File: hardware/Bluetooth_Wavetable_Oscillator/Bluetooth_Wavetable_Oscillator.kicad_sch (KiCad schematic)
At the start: 6 parts, among them U2 ESP32-C6-DevKitC-1, U3 MCP4821

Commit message: add audio test files
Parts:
- C15, C7, C8: footprint (none) -> Capacitor_THT:C_Disc_D5.0mm_W2.5mm_P5.00mm
- U3: footprint (none) -> Package_DIP:DIP-8_W7.62mm
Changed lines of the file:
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@@
 			)
 		)
-		(property "Footprint" ""
+		(property "Footprint" "Capacitor_THT:C_Disc_D5.0mm_W2.5mm_P5.00mm"
 			(at 56.8452 50.8 0)
 			(effects
@@
 			)
 		)
-		(property "Footprint" ""
+		(property "Footprint" "Package_DIP:DIP-8_W7.62mm"
 			(at 102.87 156.21 0)
 			(effects
@@
 			)
 		)
-		(property "Footprint" ""
+		(property "Footprint" "Capacitor_THT:C_Disc_D5.0mm_W2.5mm_P5.00mm"
 			(at 90.17 138.7348 0)
 			(effects
@@
 			)
 		)
-		(property "Footprint" ""
+		(property "Footprint" "Capacitor_THT:C_Disc_D5.0mm_W2.5mm_P5.00mm"
 			(at 211.7852 67.31 0)
 			(effects

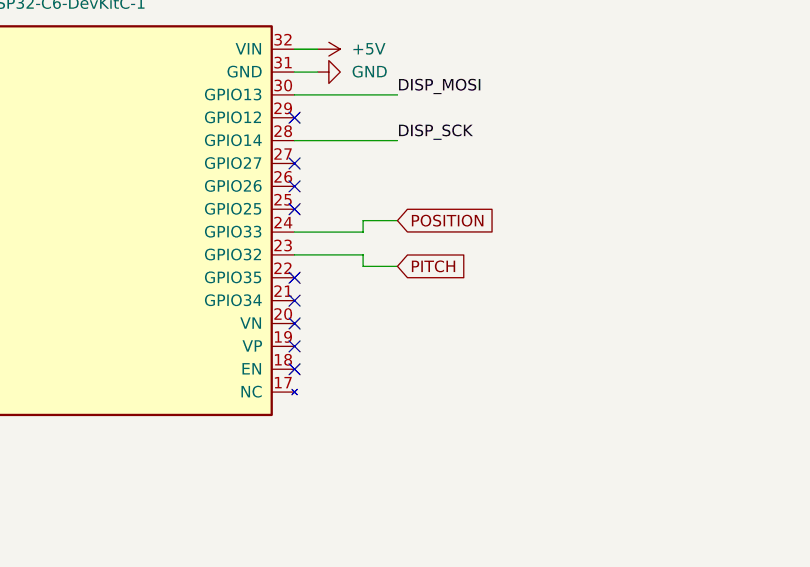
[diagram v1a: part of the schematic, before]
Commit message: change ADC input pins in schematic
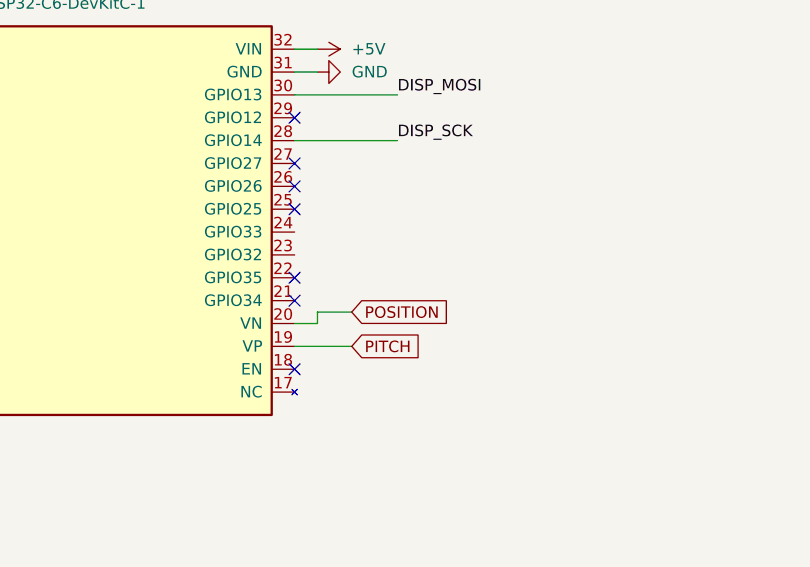
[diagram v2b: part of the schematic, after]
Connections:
- net PITCH: now also U2.19 (VP); no longer U2.23 (GPIO32)
- net POSITION: now also U2.20 (VN); no longer U2.24 (GPIO33)
- no-connect marks 16 -> 14
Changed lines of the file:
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@@
-	)
-	(no_connect
-		(at 109.22 83.82)
 	)
 	(no_connect
@@
 	)
 	(no_connect
-		(at 109.22 86.36)
-	)
-	(no_connect
 		(at 109.22 68.58)
 	)
 	(wire
 		(pts
+			(xy 109.22 86.36) (xy 115.57 86.36)
+		)
+		(stroke
+			(width 0)
+			(type default)
+		)
+	)
+	(wire
+		(pts
 			(xy 45.72 158.75) (xy 67.31 158.75)
 		)
@@
 	(wire
 		(pts
-			(xy 109.22 76.2) (xy 116.84 76.2)
-		)
-		(stroke
-			(width 0)
-			(type default)
-		)
-	)
-	(wire
-		(pts
 			(xy 109.22 58.42) (xy 120.65 58.42)
 		)
@@
 	(wire
 		(pts
+			(xy 111.76 82.55) (xy 111.76 83.82)
+		)
+		(stroke
+			(width 0)
+			(type default)
+		)
+	)
+	(wire
+		(pts
 			(xy 55.88 40.64) (xy 55.88 43.18)
 		)
@@
 	(wire
 		(pts
-			(xy 116.84 73.66) (xy 109.22 73.66)
-		)
-		(stroke
-			(width 0)
-			(type default)
-		)
-	)
-	(wire
-		(pts
 			(xy 95.25 153.67) (xy 104.14 153.67)
 		)
@@
 	(wire
 		(pts
-			(xy 116.84 76.2) (xy 116.84 77.47)
+			(xy 111.76 83.82) (xy 109.22 83.82)
 		)
 		(stroke
@@
 	(wire
 		(pts
-			(xy 116.84 72.39) (xy 120.65 72.39)
-		)
-		(stroke
-			(width 0)
-			(type default)
-		)
-	)
-	(wire
-		(pts
 			(xy 53.34 53.34) (xy 55.88 53.34)
 		)
@@
 	(wire
 		(pts
-			(xy 116.84 77.47) (xy 120.65 77.47)
-		)
-		(stroke
-			(width 0)
-			(type default)
-		)
-	)
-	(wire
-		(pts
 			(xy 213.36 83.82) (xy 226.06 83.82)
 		)
@@
 	(wire
 		(pts
+			(xy 115.57 82.55) (xy 111.76 82.55)
+		)
+		(stroke
+			(width 0)
+			(type default)
+		)
+	)
+	(wire
+		(pts
 			(xy 55.88 53.34) (xy 58.42 53.34)
 		)
@@
 		(pts
 			(xy 80.01 139.7) (xy 82.55 139.7)
-		)
-		(stroke
-			(width 0)
-			(type default)
-		)
-	)
-	(wire
-		(pts
-			(xy 116.84 72.39) (xy 116.84 73.66)
 		)
 		(stroke
@@
 	(global_label "POSITION"
 		(shape input)
-		(at 120.65 72.39 0)
+		(at 115.57 82.55 0)
 		(fields_autoplaced yes)
 		(effects
@@
 		)
 		(property "Intersheetrefs" "${INTERSHEET_REFS}"
-			(at 132.2834 72.39 0)
+			(at 127.2034 82.55 0)
 			(effects
 				(font
@@
 	(global_label "PITCH"
 		(shape input)
-		(at 120.65 77.47 0)
+		(at 115.57 86.36 0)
 		(fields_autoplaced yes)
 		(effects
@@
 		)
 		(property "Intersheetrefs" "${INTERSHEET_REFS}"
-			(at 129.0781 77.47 0)
+			(at 123.9981 86.36 0)
 			(effects
 				(font

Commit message: add bth components, add component values, update SPI pins, change disp power supply to 5V
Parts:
- added D7: LED, symbol Device:LED
- added R23: R, symbol Device:R
- added SW1: SW_Push, symbol Switch:SW_Push
- C15: value C -> 0.1u
- U2: value ESP32-C6-DevKitC-1 -> ESP32-WROOM-32D
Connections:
- net +3.3V: no longer C15.2, DISP1.2 (VDD)
- net +5V: now also C15.2, DISP1.2 (VDD)
- net DAC_CS: now also U2.3 (GPIO15); no longer U2.8 (GPIO5)
- net DAC_MOSI: now also U2.30 (GPIO13); no longer U2.15 (GPIO23)
- net DAC_SCK: now also U2.28 (GPIO14); no longer U2.9 (GPIO18)
- net DISP_CS: now also U2.8 (GPIO5); no longer U2.3 (GPIO15)
- net DISP_MOSI: now also U2.15 (GPIO23); no longer U2.30 (GPIO13)
- net DISP_SCK: now also U2.9 (GPIO18); no longer U2.28 (GPIO14)
- net GND: now also R23.2, SW1.1
- net BTH_LED: now reaches U2.14 (GPIO22)
- net BTH_LED: now also D7.2 (A)
- net BTH_SWITCH: now reaches U2.5 (GPIO4)
- net BTH_SWITCH: now also SW1.2
- new net: D7.1 (K), R23.1
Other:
- moved on the sheet: C15

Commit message: start PCB layout
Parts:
- D7: footprint (none) -> Diode_THT:D_A-405_P2.54mm_Vertical_AnodeUp
- DISP1: footprint (none) -> 1.5inch_RGB_OLED_Module:1.5inch_RGB_OLED_Module
- R23: value R -> 220R; footprint (none) -> Resistor_THT:R_Axial_DIN0204_L3.6mm_D1.6mm_P2.54mm_Vertical
- SW1: footprint (none) -> 6Pin-Switch-Button:6Pin-Switch-Button
- U2: footprint (none) -> ESP32:ESP32
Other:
- title: Microcontroller, DAC, Display -> Microcontroller, DAC, Display, BTH Switch/LED
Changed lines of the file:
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@@
 	(paper "A4")
 	(title_block
-		(title "Microcontroller, DAC, Display")
+		(title "Microcontroller, DAC, Display, BTH Switch/LED")
 		(date "2024-11-18")
 		(rev "1")
@@
 			)
 		)
-		(property "Footprint" ""
+		(property "Footprint" "1.5inch_RGB_OLED_Module:1.5inch_RGB_OLED_Module"
 			(at 232.41 72.39 0)
 			(effects
@@
 			)
 		)
-		(property "Footprint" ""
+		(property "Footprint" "ESP32:ESP32"
 			(at 83.82 96.52 0)
 			(effects
@@
 			)
 		)
-		(property "Value" "R"
+		(property "Value" "220R"
 			(at 234.95 135.89 90)
 			(effects
@@
 			)
 		)
-		(property "Footprint" ""
+		(property "Footprint" "Resistor_THT:R_Axial_DIN0204_L3.6mm_D1.6mm_P2.54mm_Vertical"
 			(at 234.95 141.478 90)
 			(effects
@@
 			)
 		)
-		(property "Footprint" ""
+		(property "Footprint" "Diode_THT:D_A-405_P2.54mm_Vertical_AnodeUp"
 			(at 222.25 139.7 0)
 			(effects
@@
 			)
 		)
-		(property "Footprint" ""
+		(property "Footprint" "6Pin-Switch-Button:6Pin-Switch-Button"
 			(at 222.25 115.57 0)
 			(effects
